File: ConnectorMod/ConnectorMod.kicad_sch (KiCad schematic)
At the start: 74 parts, among them J1 PJ-325, J2 PJ-325, J3 PJ-325, J4 PJ-066A, J5 BAT1, J6 BAT2, Q1 MMBT3906, Q2 MMBT3906, Q3 MMBT3906, Q4 MMBT3904, Q5 MMBT3904, U1 TLV2372, U2 TLP2366

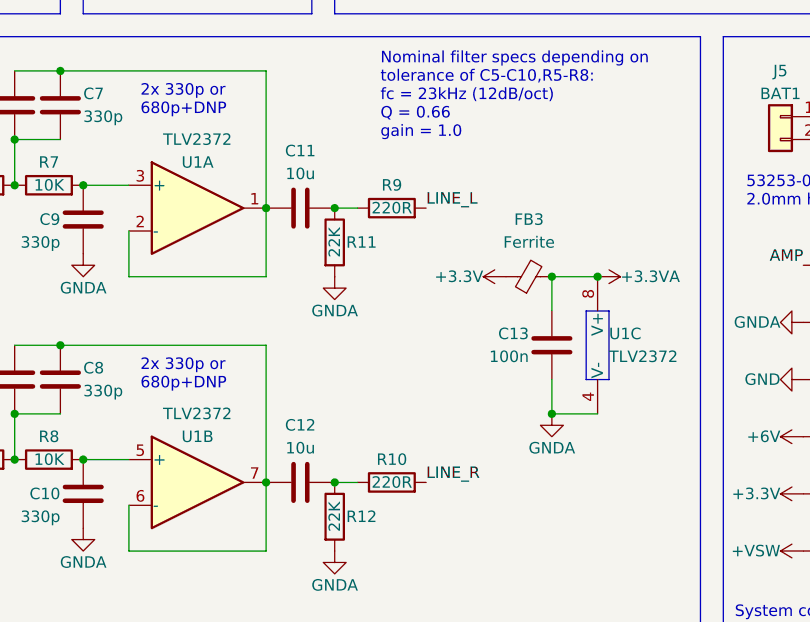
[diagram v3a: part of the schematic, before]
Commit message: Tidy up opamp circuit
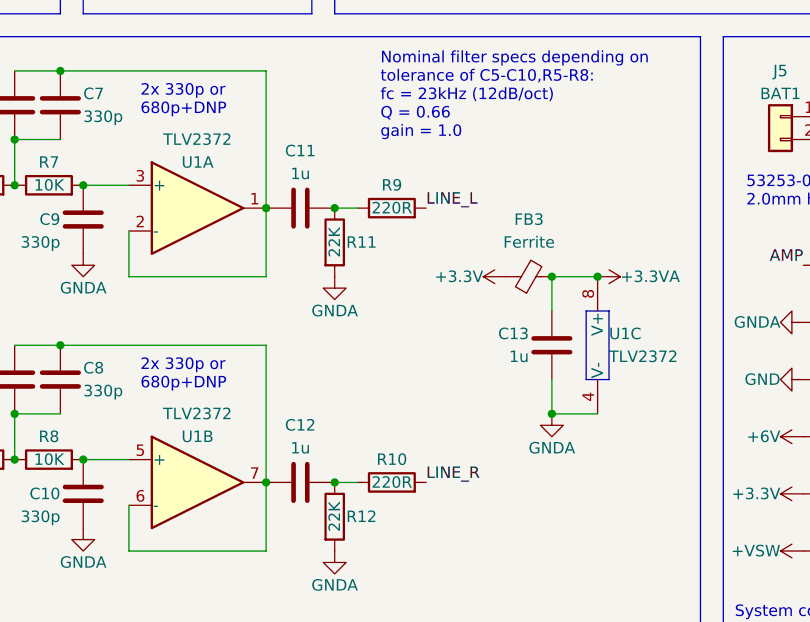
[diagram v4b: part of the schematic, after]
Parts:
- C11, C12: value 10u -> 1u
- C13: value 100n -> 1u; footprint Capacitor_SMD:C_0603_1608Metric -> Capacitor_SMD:C_0805_2012Metric
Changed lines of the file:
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@@
+    )
+  )
+  (symbol (lib_id "Device:C") (at 167.64 86.36 0) (unit 1)
+    (in_bom yes) (on_board yes) (dnp no)
+    (property "Reference" "C13" (at 165.1 85.09 0)
+      (effects (font (size 1.27 1.27)) (justify right))
+    )
+    (property "Value" "1u" (at 165.1 87.63 0)
+      (effects (font (size 1.27 1.27)) (justify right))
+    )
+    (property "Footprint" "Capacitor_SMD:C_0805_2012Metric" (at 168.6052 90.17 0)
+      (effects (font (size 1.27 1.27)) hide)
+    )
+    (property "Datasheet" "~" (at 167.64 86.36 0)
+      (effects (font (size 1.27 1.27)) hide)
+    )
+    (pin "1")
+    (pin "2")
+    (instances
+      (project "ConnectorMod"
+        (path "/e3354e21-de42-44dd-8282-d614b334b32b"
+          (reference "C13") (unit 1)
+        )
+      )
     )
   )
@@
     )
   )
-  (symbol (lib_id "Device:C") (at 167.64 86.36 0) (unit 1)
-    (in_bom yes) (on_board yes) (dnp no)
-    (property "Reference" "C13" (at 165.1 85.09 0)
-      (effects (font (size 1.27 1.27)) (justify right))
-    )
-    (property "Value" "100n" (at 165.1 87.63 0)
-      (effects (font (size 1.27 1.27)) (justify right))
-    )
-    (property "Footprint" "Capacitor_SMD:C_0603_1608Metric" (at 168.6052 90.17 0)
-      (effects (font (size 1.27 1.27)) hide)
-    )
-    (property "Datasheet" "~" (at 167.64 86.36 0)
-      (effects (font (size 1.27 1.27)) hide)
-    )
-    (pin "1")
-    (pin "2")
-    (instances
-      (project "ConnectorMod"
-        (path "/e3354e21-de42-44dd-8282-d614b334b32b"
-          (reference "C13") (unit 1)
-        )
-      )
-    )
-  )
   (symbol (lib_id "Device:R") (at 111.76 68.58 90) (unit 1)
     (in_bom yes) (on_board yes) (dnp no)
@@
       (effects (font (size 1.27 1.27)))
     )
-    (property "Value" "10u" (at 139.7 67.31 90)
+    (property "Value" "1u" (at 139.7 67.31 90)
       (effects (font (size 1.27 1.27)))
     )
@@
       (effects (font (size 1.27 1.27)))
     )
-    (property "Value" "10u" (at 139.7 97.79 90)
-      (effects (font (size 1.27 1.27)))
-    )
+    (property "Value" "1u" (at 139.7 97.79 90)
+      (effects (font (size 1.27 1.27)))
+    )

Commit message: Make all audio caps at least 0805
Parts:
- C10, C3, C4, C5, C6, C7, C8, C9: footprint Capacitor_SMD:C_0603_1608Metric -> Capacitor_SMD:C_0805_2012Metric
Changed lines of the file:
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@@
       (effects (font (size 1.27 1.27)))
     )
-    (property "Footprint" "Capacitor_SMD:C_0603_1608Metric" (at 90.17 67.6148 0)
+    (property "Footprint" "Capacitor_SMD:C_0805_2012Metric" (at 90.17 67.6148 0)
       (effects (font (size 1.27 1.27)) hide)
     )
@@
       (effects (font (size 1.27 1.27)) (justify left))
     )
-    (property "Footprint" "Capacitor_SMD:C_0603_1608Metric" (at 113.9952 63.5 0)
+    (property "Footprint" "Capacitor_SMD:C_0805_2012Metric" (at 113.9952 63.5 0)
       (effects (font (size 1.27 1.27)) hide)
     )
@@
       (effects (font (size 1.27 1.27)) (justify right))
     )
-    (property "Footprint" "Capacitor_SMD:C_0603_1608Metric" (at 116.5352 106.68 0)
+    (property "Footprint" "Capacitor_SMD:C_0805_2012Metric" (at 116.5352 106.68 0)
       (effects (font (size 1.27 1.27)) hide)
     )
@@
       (effects (font (size 1.27 1.27)))
     )
-    (property "Footprint" "Capacitor_SMD:C_0603_1608Metric" (at 90.17 98.0948 0)
+    (property "Footprint" "Capacitor_SMD:C_0805_2012Metric" (at 90.17 98.0948 0)
       (effects (font (size 1.27 1.27)) hide)
     )
@@
       (effects (font (size 1.27 1.27)) (justify left))
     )
-    (property "Footprint" "Capacitor_SMD:C_0603_1608Metric" (at 113.9952 93.98 0)
+    (property "Footprint" "Capacitor_SMD:C_0805_2012Metric" (at 113.9952 93.98 0)
       (effects (font (size 1.27 1.27)) hide)
     )
@@
       (effects (font (size 1.27 1.27)) (justify right))
     )
-    (property "Footprint" "Capacitor_SMD:C_0603_1608Metric" (at 108.9152 93.98 0)
+    (property "Footprint" "Capacitor_SMD:C_0805_2012Metric" (at 108.9152 93.98 0)
       (effects (font (size 1.27 1.27)) hide)
     )
@@
       (effects (font (size 1.27 1.27)) (justify right))
     )
-    (property "Footprint" "Capacitor_SMD:C_0603_1608Metric" (at 108.9152 63.5 0)
+    (property "Footprint" "Capacitor_SMD:C_0805_2012Metric" (at 108.9152 63.5 0)
       (effects (font (size 1.27 1.27)) hide)
     )
@@
       (effects (font (size 1.27 1.27)) (justify right))
     )
-    (property "Footprint" "Capacitor_SMD:C_0603_1608Metric" (at 116.5352 76.2 0)
-      (effects (font (size 1.27 1.27)) hide)
-    )
+    (property "Footprint" "Capacitor_SMD:C_0805_2012Metric" (at 116.5352 76.2 0)
+      (effects (font (size 1.27 1.27)) hide)
+    )
